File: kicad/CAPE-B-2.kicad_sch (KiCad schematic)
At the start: 30 parts, among them SW1 SW_DIP_x02, X2Y_CAN 4.7nF_X2Y, X2Y_RS485 4.7nF_X2Y

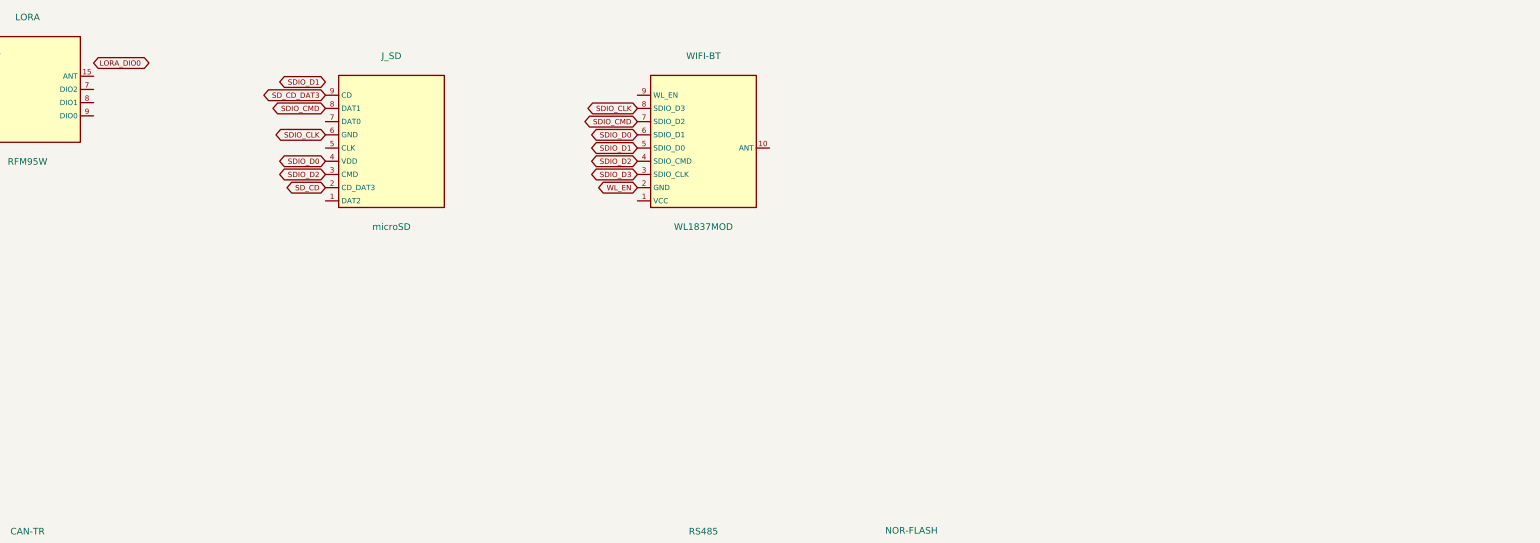
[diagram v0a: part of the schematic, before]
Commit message: avionics/CAPE-B-2: add §13 antenna filter chains (EMI hardening)
Each on-board RF transceiver now has a dedicated filtered antenna path:
- FL_LORA / FL_SIK: Johanson 0915LP15B0100E BPF (902–928 MHz, 0.6 dB IL)
- FL_WIFI: Johanson 2450BP15B050E BPF (2400–2500 MHz, 0.5 dB IL)
- D_ANT_LORA / D_ANT_WIFI / D_ANT_SIK: Semtech RCLAMP0502BTCL ESD shunt
  (0.15 pF — chosen to avoid antenna detuning at 915 / 2400 MHz)
- J_SMA_LORA / J_SMA_WIFI / J_SMA_SIK: SMA PCB bulkhead jacks, shells to PGND
- J_SIK_ANT: Hirose U.FL-R-SMT-1 pad receives SiK RFD900x module pigtail

New lib_symbols: PGND, BPF_915, BPF_2400, RCLAMP0502B, Conn_SMA, Conn_UFL
LORA_ANT and WIFI_ANT global net labels added at module ANT pins.
CAPE-B-2.md updated with §13 topology, component rationale, PCB constraints,
BOM delta, and references. TODO.md line 175 marked complete.

References: Johanson 0915LP15B0100E DS; Johanson 2450BP15B050E DS;
Semtech RCLAMP0502B DS (RF ESD, 0.15 pF max capacitance).
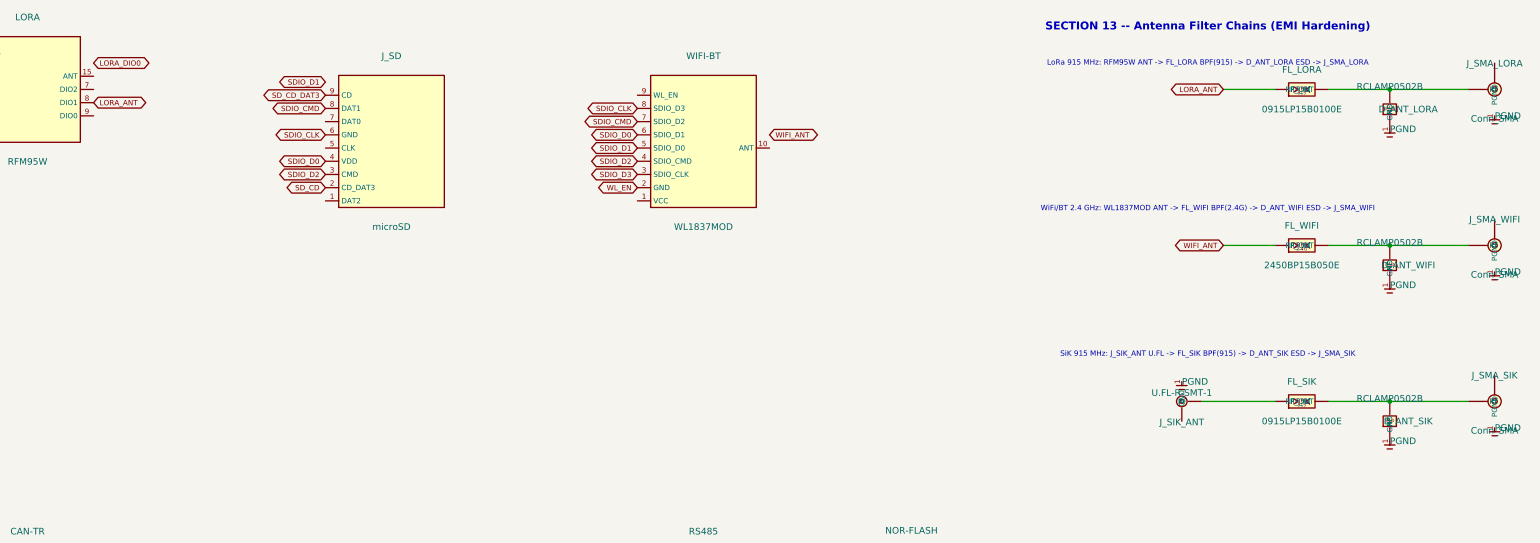
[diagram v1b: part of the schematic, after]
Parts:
- added D_ANT_LORA, D_ANT_SIK, D_ANT_WIFI: RCLAMP0502B, Diode_SMD:D_SOD-882, symbol RCLAMP0502B
- added FL_LORA, FL_SIK: 0915LP15B0100E, Filter:BPF_1206, symbol BPF_915
- added FL_WIFI: 2450BP15B050E, Filter:BPF_1206, symbol BPF_2400
- added J_SIK_ANT: U.FL-R-SMT-1, Connector_Coaxial:U.FL_Hirose_UFL-R-SMT-1_Vertical, symbol Conn_UFL
- added J_SMA_LORA, J_SMA_SIK, J_SMA_WIFI: Conn_SMA, Connector_Coaxial:SMA_Vertical_Straight, symbol Conn_SMA
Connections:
- net LORA_ANT: now reaches LORA.8 (DIO1)
- net LORA_ANT: now also FL_LORA.1 (RF_IN)
- new net: D_ANT_LORA.2 (GND), FL_LORA.2 (RF_OUT), J_SMA_LORA.1 (RF)
- new net: D_ANT_WIFI.2 (GND), FL_WIFI.2 (RF_OUT), J_SMA_WIFI.1 (RF)
- new net: FL_SIK.1 (RF_IN), J_SIK_ANT.1 (RF)
- new net: D_ANT_SIK.2 (GND), FL_SIK.2 (RF_OUT), J_SMA_SIK.1 (RF)
- new net PGND: D_ANT_LORA.1 (RF), D_ANT_SIK.1 (RF), D_ANT_WIFI.1 (RF)
- new net WIFI_ANT: FL_WIFI.1 (RF_IN)
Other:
- note added: "LoRa 915 MHz: RFM95W ANT -> FL_LORA BPF(915) -> D_ANT_LORA ESD -> J_SMA_LORA"
- note added: "SECTION 13 -- Antenna Filter Chains (EMI Hardening)"
- note added: "SiK 915 MHz: J_SIK_ANT U.FL -> FL_SIK BPF(915) -> D_ANT_SIK ESD -> J_SMA_SIK"
- note added: "WiFi/BT 2.4 GHz: WL1837MOD ANT -> FL_WIFI BPF(2.4G) -> D_ANT_WIFI ESD -> J_SMA_WIFI"

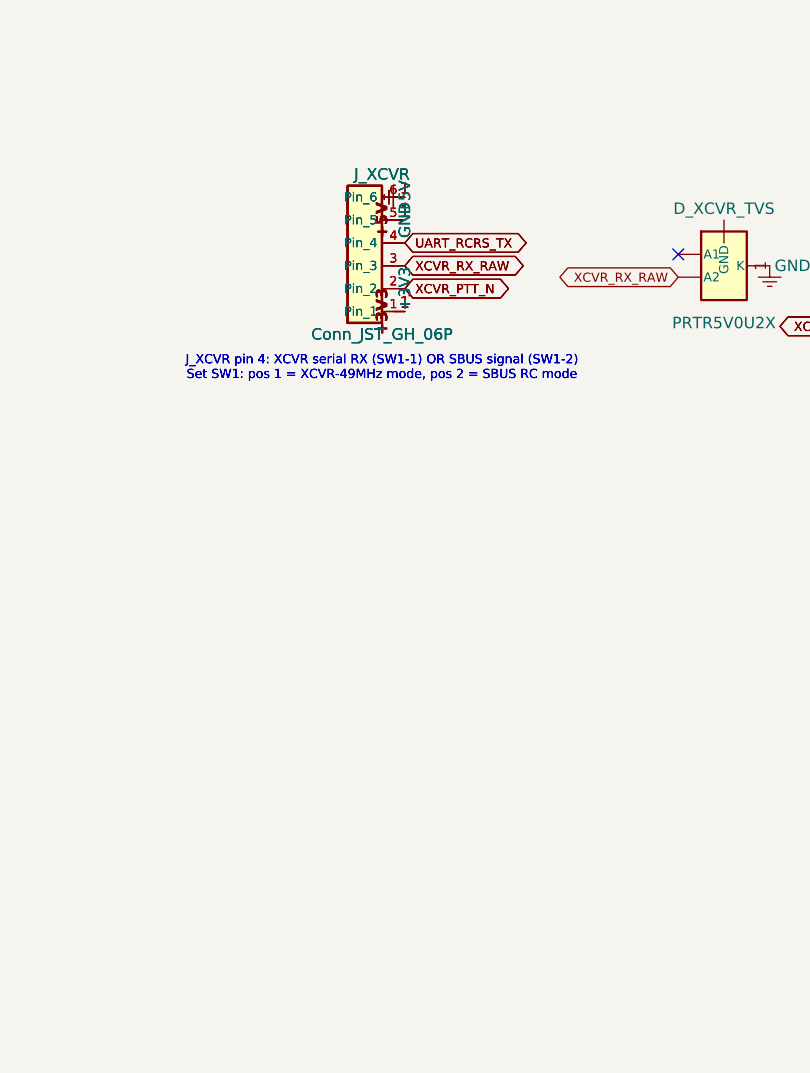
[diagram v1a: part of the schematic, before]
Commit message: Add shielded JST-GH connectors, wiring harness spec, Faraday enclosure, and bay fans
Schematics (Cape-A-2, Cape-B-2, XCVR-49MHZ-2):
- Added SHIELD/MP pin to all JST-GH connector symbol definitions, bonded to PGND
- Added PGND power symbol definition to each schematic's lib_symbols
- Added pin "MP" UUID to all connector instances (J_VBAT, J_SBUS, J_XCVR, J1)
- Added PGND power symbol instance at each connector's MP mounting-tab pad
- Added J_FAN 3-pin JST-GH connector to Cape-A-2 and Cape-B-2
  (GND / +5V / FAN_PWM_A|B + PGND shield bond)
- Added Conn_JST_GH_03P symbol definition to Cape-B-2 lib_symbols

Design docs:
- Cape-A-2.md §9: Shielded JST-GH connector spec (cable type, drain wire, ferrite)
- Cape-A-2.md §10: J_FAN fan connector spec (Sunon MF40100V2, 5 V, PWM)
- Cape-A-2.md §11: Wiring harness requirements — all cables twisted+shielded+ferrite
  (CAN FD / RS-485 / 1553 / PWM / power / Ethernet / SBUS / fan)
- Cape-A-2.md §12: Avionics bay Faraday enclosure — 3M 1181 copper foil liner,
  Laird HCZ0-2050-A 40 mm honeycomb EMC vent, fan frame PGND bond, access-panel
  conductive foam gaskets, cable entry ferrite clamps; SE ≥ 30 dB @ 49 MHz
- Cape-B-2.md: Matching shielded connector spec, J_FAN, wiring requirements,
  Faraday enclosure addenda (XCVR SMA bulkhead, RF antenna pigtail routing)
- XCVR-49MHZ-2.md §8: J1 shielded cable assembly spec, drain wire, ferrite clamp
  placement; SMA antenna cable spec; wiring interaction with on-board CM5/TVS6/FB-TX

Ref: Cape-A-2.md §12.5 (SE budget), IEC 61000-4-2/4-5, MIL-STD-461G RS103

https://claude.ai/code/session_01PLmQi3tDwTStFSfcJLQJp7
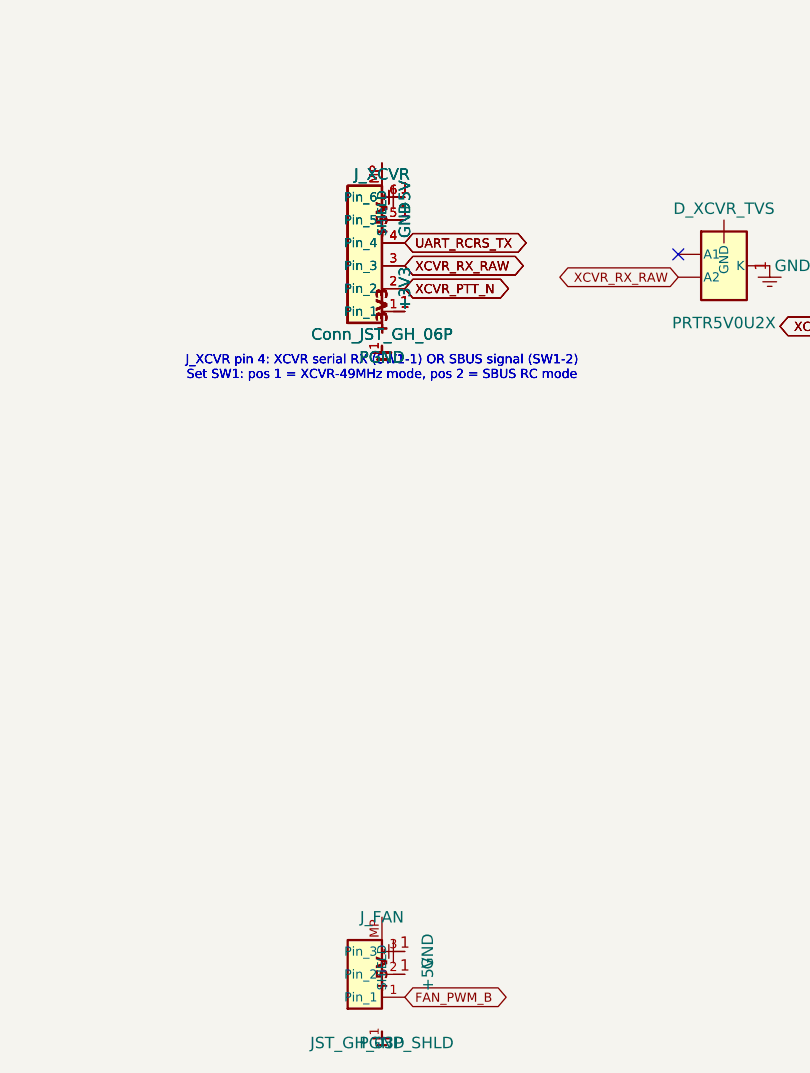
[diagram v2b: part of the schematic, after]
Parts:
- added J_FAN: JST_GH_03P_SHLD, Connector_JST:JST_GH_SM03B-GHS-TB_1x03-1MP_P1.25mm_Horizontal, symbol Conn_JST_GH_03P
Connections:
- net +5V: now also J_FAN.2 (Pin_2)
- net GND: now also J_FAN.3 (Pin_3)
- new net FAN_PWM_B: J_FAN.1 (Pin_1)
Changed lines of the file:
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@@
     (pin "5")
     (pin "6")
+    (pin "MP")
+  )
+  (symbol (lib_id "PGND") (at 100.00 570.16 0)
+    (unit 1) (exclude_from_sim no) (in_bom no) (on_board yes) (dnp no)
+    (property "Reference" "#PWR_XCVR_SHLD" (at 100.00 570.16 0) (effects (font (size 1.27 1.27)) (hide yes)))
+    (property "Value" "PGND" (at 100.00 571.43 0) (effects (font (size 1.27 1.27))))
+    (pin "1")
   )
   (symbol (lib_id "GND") (at 102.54 553.65 270)
@@
     (pin "5")
     (pin "6")
+    (pin "MP")
+  )
+  (symbol (lib_id "PGND") (at 100.00 570.16 0)
+    (unit 1) (exclude_from_sim no) (in_bom no) (on_board yes) (dnp no)
+    (property "Reference" "#PWR_XCVR_SHLD" (at 100.00 570.16 0) (effects (font (size 1.27 1.27)) (hide yes)))
+    (property "Value" "PGND" (at 100.00 571.43 0) (effects (font (size 1.27 1.27))))
+    (pin "1")
   )
   (symbol (lib_id "GND") (at 102.54 553.65 270)
@@
     (pin "1")
   )
+  (symbol (lib_id "Conn_JST_GH_03P") (at 100.00 640.00 0)
+    (unit 1) (exclude_from_sim no) (in_bom yes) (on_board yes) (dnp no)
+    (property "Reference" "J_FAN" (at 100.00 633.65 0) (effects (font (size 1.27 1.27))))
+    (property "Value" "JST_GH_03P_SHLD" (at 100.00 647.62 0) (effects (font (size 1.27 1.27))))
+    (property "Footprint" "Connector_JST:JST_GH_SM03B-GHS-TB_1x03-1MP_P1.25mm_Horizontal" (at 0 0 0) (effects (font (size 1.27 1.27)) (hide yes)))
+    (property "Datasheet" "https://www.jst.com/wp-content/uploads/2021/01/eGH.pdf" (at 0 0 0) (effects (font (size 1.27 1.27)) (hide yes)))
+    (pin "1")
+    (pin "2")
+    (pin "3")
+    (pin "MP")
+  )
+  (symbol (lib_id "GND") (at 102.54 637.46 270)
+    (unit 1) (exclude_from_sim no) (in_bom no) (on_board yes) (dnp no)
+    (property "Reference" "#PWR_FAN_GND" (at 102.54 637.46 0) (effects (font (size 1.27 1.27)) (hide yes)))
+    (property "Value" "GND" (at 105.08 637.46 0) (effects (font (size 1.27 1.27))))
+    (pin "1")
+  )
+  (symbol (lib_id "+5V") (at 102.54 640.00 90)
+    (unit 1) (exclude_from_sim no) (in_bom no) (on_board yes) (dnp no)
+    (property "Reference" "#PWR_FAN_5V" (at 102.54 640.00 0) (effects (font (size 1.27 1.27)) (hide yes)))
+    (property "Value" "+5V" (at 105.08 640.00 0) (effects (font (size 1.27 1.27))))
+    (pin "1")
+  )
+  (global_label "FAN_PWM_B" (shape bidirectional) (at 102.54 642.54 0)
+    (effects (font (size 1.016 1.016)))
+    (property "Intersheet References" "${INTERSHEET_REFS}" (at 102.54 642.54 0)
+      (effects (font (size 1.016 1.016)) (hide yes))))
+  (symbol (lib_id "PGND") (at 100.00 646.35 0)
+    (unit 1) (exclude_from_sim no) (in_bom no) (on_board yes) (dnp no)
+    (property "Reference" "#PWR_FAN_SHLD" (at 100.00 646.35 0) (effects (font (size 1.27 1.27)) (hide yes)))
+    (property "Value" "PGND" (at 100.00 647.62 0) (effects (font (size 1.27 1.27))))
+    (pin "1")
+  )

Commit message: Rev Q: Wash/Zoë Ethernet PHYs, field connectors, Rev Q documentation propagation
Implements TODO tasks 1.4.2–1.4.5 and 1.5.1. Renames Cape-B-2 callsign
from "Mr. Universe" to "Zoë" throughout per CLAUDE.md (2026-06-07).

Wash (CAPE-A-2) — task 1.4.2 + 1.4.4:
- Dual EMI-hardened Ethernet PHY: DP83825I ×2 (RMII0→PHY1 addr 0x01,
  RMII1→PHY2 addr 0x02); HX1188NL magnetics ×2; TPS62933 1.8V ×2;
  PRTR5V0U2X TVS ×4; SRF2012-100Y CMC ×2; J_ETH1 + J_ETH2 (SM06B-GHS)
- Field connectors: J_PWR, J_CAN (CAN_A_H/L), J_485 (RS485_A_P/N),
  J_1553 (BUS_1553_A_P/N), J_GPS, J_SERVO (CH0–CH3), J_ESC (ESC_PWM_0–2)
- All connector MPs → PGND star; title block: rev Q, date 2026-06-07
- CAPE-A-2.md: §14 field connector summary table added

Zoë (CAPE-B-2) — task 1.4.3 + 1.4.5:
- Rename from "Mr. Universe" to "Zoë" in schematic title, .md, TODO.md
- Single EMI-hardened Ethernet PHY (RMII0, PHY addr 0x01); J_ETH_B
- Field connectors: J_PWR, J_CAN (CAN_B_H/L), J_485 (RS485_B_P/N),
  J_1553 (BUS_1553_B_P/N) — _B_ suffix prevents bus-ring net collisions
- CAPE-B-2.md: §14 field connector summary table added

TODO.md — task 1.5.1 + merge conflict resolution:
- Rev Q propagation: node placement v2·v2·v2·v2, procurement 4×Wash +
  4×Zoë + 4×XCVR-49MHZ-2, Phase 6/7 installation steps updated
- Tasks 1.4.2–1.4.5 and 1.5.1 marked done
- Merge conflict resolved (Rev Q header retained; user's new open tasks
  for Cape-A-2 PCB finish, SBUS/UART DIP, Zoë ETH2 re-evaluation kept)

https://claude.ai/code/session_01PLmQi3tDwTStFSfcJLQJp7
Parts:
- removed J_FAN: JST_GH_03P_SHLD, Connector_JST:JST_GH_SM03B-GHS-TB_1x03-1MP_P1.25mm_Horizontal, symbol Conn_JST_GH_03P
- added CM_ETH_B: SRF2012-100Y, Inductor_SMD:L_0805_2012Metric, symbol SRF2012
- added ETH_PHY_B: DP83825I, Package_QFP:LQFP-32_7x7mm_P0.8mm, symbol DP83825I
- added HX1188_B: HX1188NL, Package_SO:SOIC-16_3.9x9.9mm_P1.27mm, symbol HX1188NL
- added J_1553: SM04B-GHS-TB-1MP — MIL-STD-1553B, Connector_JST:JST_GH_SM04B-GHS-TB_1x04-1MP_P1.25mm_Horizontal, symbol Conn_JST_GH_04P
- added J_485: SM03B-GHS-TB-1MP — RS-485, Connector_JST:JST_GH_SM03B-GHS-TB_1x03-1MP_P1.25mm_Horizontal, symbol Conn_JST_GH_03P
- added J_CAN: SM03B-GHS-TB-1MP — CAN FD, Connector_JST:JST_GH_SM03B-GHS-TB_1x03-1MP_P1.25mm_Horizontal, symbol Conn_JST_GH_03P
- added J_ETH_B: SM06B-GHS-TB-1MP, Connector_JST:JST_GH_SM06B-GHS-TB_1x06-1MP_P1.25mm_Horizontal, symbol Conn_JST_GH_06P
- added J_PWR: JST_GH_04P — Power Input, Connector_JST:JST_GH_SM04B-GHS-TB_1x04-1MP_P1.25mm_Horizontal, symbol Conn_JST_GH_04P
- added R_RBIAS_B: 49.9R_1%, Resistor_SMD:R_0402_1005Metric, symbol R_SMD
- added TVS_ETHB_RX, TVS_ETHB_TX: PRTR5V0U2X, Package_TO_SOT_SMD:SOT-363_SC-70-6, symbol PRTR5V0U2X
- added U_ETH_B_1V8: TPS62933, Package_SO:SOIC-8_3.9x4.9mm_P1.27mm, symbol TPS62933
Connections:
- new net ETHB_RX_N: J_ETH_B.3 (Pin_3)
- new net ETHB_RX_P: J_ETH_B.4 (Pin_4)
- new net ETHB_TX_N: J_ETH_B.5 (Pin_5)
- new net ETHB_TX_P: J_ETH_B.6 (Pin_6)
- new net RMIB_CRSDV: ETH_PHY_B.11 (CRS_DV)
- new net RMIB_TXD0: ETH_PHY_B.1 (TXD0)
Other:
- title: CAPE-B-2 EMI-Hardened Comms, Logging & Payload Cape -> Zoë (CAPE-B-2) EMI-Hardened Comms, Logging & Payload Cape
